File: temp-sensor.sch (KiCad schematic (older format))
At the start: 5 parts

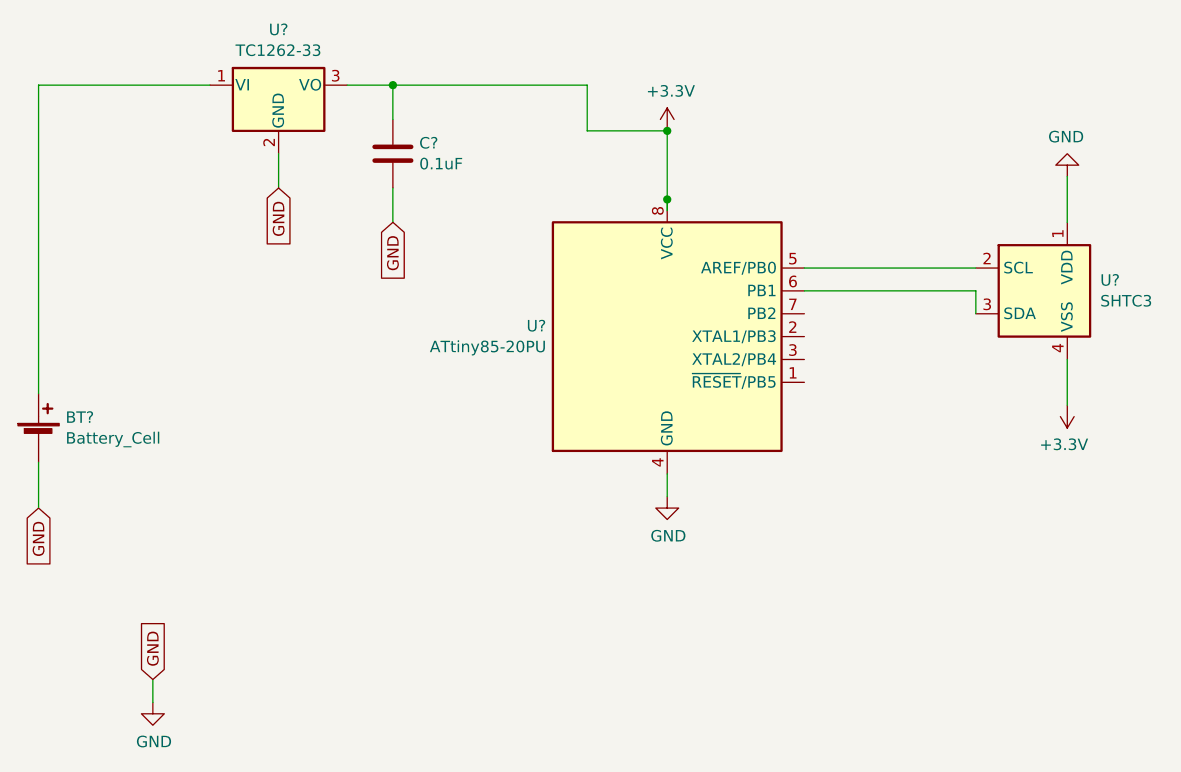
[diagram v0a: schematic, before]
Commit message: remove attiny85 (use esp01)
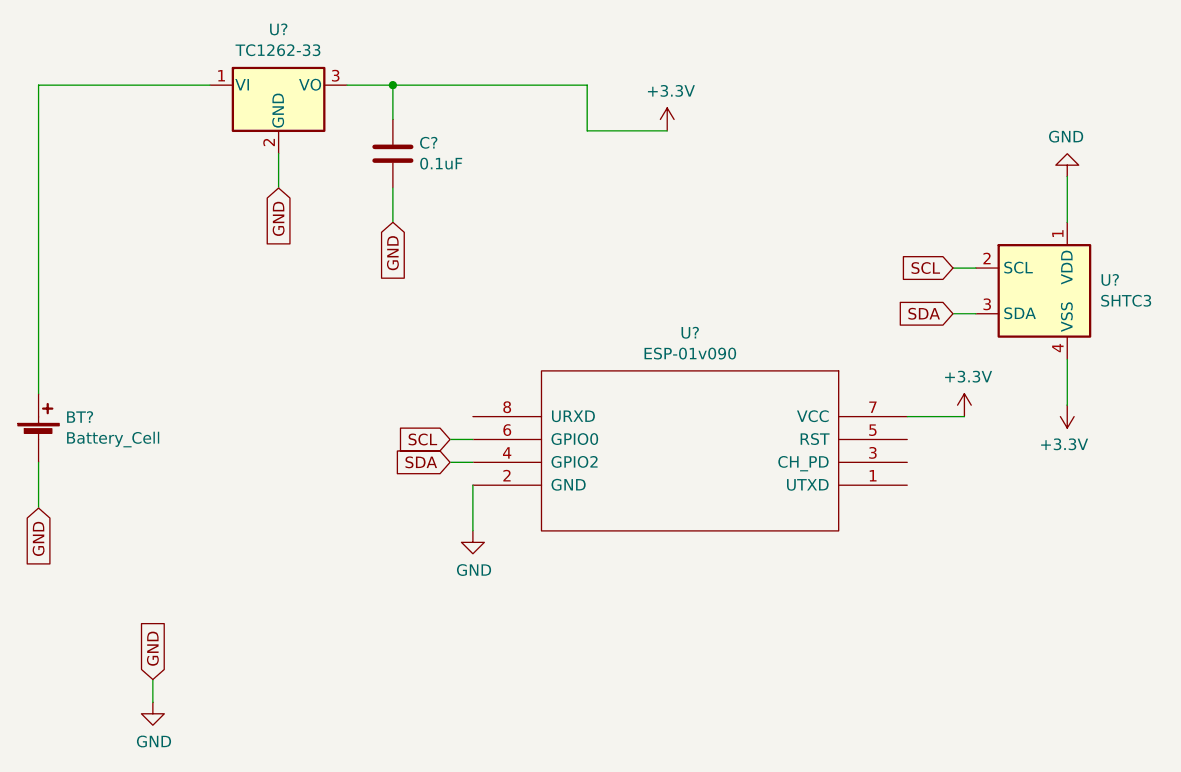
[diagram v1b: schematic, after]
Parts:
- removed U?: ATtiny85-20PU, Package_DIP:DIP-8_W7.62mm, symbol MCU_Microchip_ATtiny:ATtiny85-20PU
- added U?: ESP-01v090, symbol ESP8266:ESP-01v090
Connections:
- net labels added: SCL, SDA
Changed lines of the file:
@@
 Title "Temparature Sensor + Wifi + Attiny85"
 Date "2021-11-30"
-Rev "1"
+Rev "2"
 Comp "Kalan"
 Comment1 ""
@@
 F 3 "~" V 2000 3260 50  0001 C CNN
 	1    2000 3200
-	1    0    0    -1
-$EndComp
-$Comp
-L MCU_Microchip_ATtiny:ATtiny85-20PU U?
-U 1 1 61A69749
-P 4750 2750
-F 0 "U?" H 4221 2796 50  0000 R CNN
-F 1 "ATtiny85-20PU" H 4221 2705 50  0000 R CNN
-F 2 "Package_DIP:DIP-8_W7.62mm" H 4750 2750 50  0001 C CIN
-F 3 "http://ww1.microchip.com/downloads/en/DeviceDoc/atmel-2586-avr-8-bit-microcontroller-attiny25-attiny45-attiny85_datasheet.pdf" H 4750 2750 50  0001 C CNN
-	1    4750 2750
 	1    0    0    -1
 $EndComp
@@
 	1    0    0    -1
 $EndComp
-Wire Wire Line
-	4750 1850 4750 2150
 Text GLabel 2500 4250 1    50   Input ~ 0
 GND
@@
 Wire Wire Line
 	4400 1850 4750 1850
-Connection ~ 4750 1850
 Connection ~ 3550 1650
 Wire Wire Line
@@
 	1    0    0    -1
 $EndComp
-Connection ~ 4750 2150
-Wire Wire Line
-	4750 2150 4750 2200
-$Comp
-L power:GND #PWR?
-U 1 1 61A7129D
-P 4750 3450
-F 0 "#PWR?" H 4750 3200 50  0001 C CNN
-F 1 "GND" H 4755 3277 50  0000 C CNN
-F 2 "" H 4750 3450 50  0001 C CNN
-F 3 "" H 4750 3450 50  0001 C CNN
-	1    4750 3450
-	1    0    0    -1
-$EndComp
-Wire Wire Line
-	4750 3350 4750 3450
 $Comp
 L Sensor_Humidity:SHTC3 U?
@@
 	1    0    0    -1
 $EndComp
-Wire Wire Line
-	5350 2450 6100 2450
-Wire Wire Line
-	5350 2550 6100 2550
-Wire Wire Line
-	6100 2550 6100 2650
 $Comp
 L power:+3.3V #PWR?
@@
 Wire Wire Line
 	6500 2050 6500 2250
+$Comp
+L power:+3.3V #PWR?
+U 1 1 61A80EF4
+P 6050 3100
+F 0 "#PWR?" H 6050 2950 50  0001 C CNN
+F 1 "+3.3V" H 6065 3273 50  0000 C CNN
+F 2 "" H 6050 3100 50  0001 C CNN
+F 3 "" H 6050 3100 50  0001 C CNN
+	1    6050 3100
+	1    0    0    -1
+$EndComp
+Wire Wire Line
+	5800 3100 6050 3100
+$Comp
+L power:GND #PWR?
+U 1 1 61A81943
+P 3900 3600
+F 0 "#PWR?" H 3900 3350 50  0001 C CNN
+F 1 "GND" H 3905 3427 50  0000 C CNN
+F 2 "" H 3900 3600 50  0001 C CNN
+F 3 "" H 3900 3600 50  0001 C CNN
+	1    3900 3600
+	1    0    0    -1
+$EndComp
+Wire Wire Line
+	3900 3400 3900 3600
+$Comp
+L ESP8266:ESP-01v090 U?
+U 1 1 61A7D0E8
+P 4850 3250
+F 0 "U?" H 4850 2735 50  0000 C CNN
+F 1 "ESP-01v090" H 4850 2826 50  0000 C CNN
+F 2 "" H 4850 3250 50  0001 C CNN
+F 3 "http://l0l.org.uk/2014/12/esp8266-modules-hardware-guide-gotta-catch-em-all/" H 4850 3250 50  0001 C CNN
+	1    4850 3250
+	-1   0    0    1
+$EndComp
+Text GLabel 3800 3200 0    50   Input ~ 0
+SCL
+Text GLabel 3800 3300 0    50   Input ~ 0
+SDA
+Wire Wire Line
+	3800 3200 3900 3200
+Wire Wire Line
+	3800 3300 3900 3300
+Text GLabel 6000 2450 0    50   Input ~ 0
+SCL
+Wire Wire Line
+	6000 2450 6100 2450
+Text GLabel 6000 2650 0    50   Input ~ 0
+SDA
+Wire Wire Line
+	6000 2650 6100 2650
 $EndSCHEMATC

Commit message: update footprint
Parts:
- BT1: renamed from BT?; footprint (none) -> Battery:Battery_CR1225
- C1: renamed from C?; footprint (none) -> Capacitor_Tantalum_SMD:CP_EIA-3216-12_Kemet-S_Pad1.58x1.35mm_HandSolder
- U2: renamed from U?; footprint (none) -> ESP01
- gave numbers to parts that had none: 2
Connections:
- no-connect marks 0 -> 4
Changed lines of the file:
@@
 $EndDescr
 $Comp
-L Device:Battery_Cell BT?
+L Device:Battery_Cell BT1
 U 1 1 61A67C5E
 P 2000 3200
-F 0 "BT?" H 2118 3296 50  0000 L CNN
+F 0 "BT1" H 2118 3296 50  0000 L CNN
 F 1 "Battery_Cell" H 2118 3205 50  0000 L CNN
-F 2 "" V 2000 3260 50  0001 C CNN
+F 2 "Battery:Battery_CR1225" V 2000 3260 50  0001 C CNN
 F 3 "~" V 2000 3260 50  0001 C CNN
 	1    2000 3200
@@
 $EndComp
 $Comp
-L power:+3.3V #PWR?
+L power:+3.3V #PWR0101
 U 1 1 61A6AABD
 P 4750 1850
-F 0 "#PWR?" H 4750 1700 50  0001 C CNN
+F 0 "#PWR0101" H 4750 1700 50  0001 C CNN
 F 1 "+3.3V" H 4765 2023 50  0000 C CNN
 F 2 "" H 4750 1850 50  0001 C CNN
@@
 $EndComp
 $Comp
-L power:GND #PWR?
+L power:GND #PWR0102
 U 1 1 61A6B2A0
 P 2500 4350
-F 0 "#PWR?" H 2500 4100 50  0001 C CNN
+F 0 "#PWR0102" H 2500 4100 50  0001 C CNN
 F 1 "GND" H 2505 4177 50  0000 C CNN
 F 2 "" H 2500 4350 50  0001 C CNN
@@
 	2000 3300 2000 3500
 $Comp
-L Regulator_Linear:TC1262-33 U?
+L Regulator_Linear:TC1262-33 U1
 U 1 1 61A6D18E
 P 3050 1650
-F 0 "U?" H 3050 1892 50  0000 C CNN
+F 0 "U1" H 3050 1892 50  0000 C CNN
 F 1 "TC1262-33" H 3050 1801 50  0000 C CNN
 F 2 "" H 3050 1875 50  0001 C CIN
@@
 GND
 $Comp
-L Device:C C?
+L Device:C C1
 U 1 1 61A6F27A
 P 3550 1950
-F 0 "C?" H 3665 1996 50  0000 L CNN
+F 0 "C1" H 3665 1996 50  0000 L CNN
 F 1 "0.1uF" H 3665 1905 50  0000 L CNN
-F 2 "" H 3588 1800 50  0001 C CNN
+F 2 "Capacitor_Tantalum_SMD:CP_EIA-3216-12_Kemet-S_Pad1.58x1.35mm_HandSolder" H 3588 1800 50  0001 C CNN
 F 3 "~" H 3550 1950 50  0001 C CNN
 	1    3550 1950
@@
 $EndComp
 $Comp
-L Sensor_Humidity:SHTC3 U?
+L Sensor_Humidity:SHTC3 U3
 U 1 1 61A76649
 P 6400 2550
-F 0 "U?" H 6644 2596 50  0000 L CNN
+F 0 "U3" H 6644 2596 50  0000 L CNN
 F 1 "SHTC3" H 6644 2505 50  0000 L CNN
 F 2 "Sensor_Humidity:Sensirion_DFN-4-1EP_2x2mm_P1mm_EP0.7x1.6mm" H 6600 2200 50  0001 C CNN
@@
 $EndComp
 $Comp
-L power:+3.3V #PWR?
+L power:+3.3V #PWR0103
 U 1 1 61A799AE
 P 6500 3050
-F 0 "#PWR?" H 6500 2900 50  0001 C CNN
+F 0 "#PWR0103" H 6500 2900 50  0001 C CNN
 F 1 "+3.3V" H 6515 3223 50  0000 C CNN
 F 2 "" H 6500 3050 50  0001 C CNN
@@
 	6500 2850 6500 3050
 $Comp
-L power:GND #PWR?
+L power:GND #PWR0104
 U 1 1 61A7A14B
 P 6500 2050
-F 0 "#PWR?" H 6500 1800 50  0001 C CNN
+F 0 "#PWR0104" H 6500 1800 50  0001 C CNN
 F 1 "GND" H 6505 1877 50  0000 C CNN
 F 2 "" H 6500 2050 50  0001 C CNN
@@
 	6500 2050 6500 2250
 $Comp
-L power:+3.3V #PWR?
+L power:+3.3V #PWR0105
 U 1 1 61A80EF4
 P 6050 3100
-F 0 "#PWR?" H 6050 2950 50  0001 C CNN
+F 0 "#PWR0105" H 6050 2950 50  0001 C CNN
 F 1 "+3.3V" H 6065 3273 50  0000 C CNN
 F 2 "" H 6050 3100 50  0001 C CNN
@@
 	5800 3100 6050 3100
 $Comp
-L power:GND #PWR?
+L power:GND #PWR0106
 U 1 1 61A81943
 P 3900 3600
-F 0 "#PWR?" H 3900 3350 50  0001 C CNN
+F 0 "#PWR0106" H 3900 3350 50  0001 C CNN
 F 1 "GND" H 3905 3427 50  0000 C CNN
 F 2 "" H 3900 3600 50  0001 C CNN
@@
 	3900 3400 3900 3600
 $Comp
-L ESP8266:ESP-01v090 U?
+L ESP8266:ESP-01v090 U2
 U 1 1 61A7D0E8
 P 4850 3250
-F 0 "U?" H 4850 2735 50  0000 C CNN
+F 0 "U2" H 4850 2735 50  0000 C CNN
 F 1 "ESP-01v090" H 4850 2826 50  0000 C CNN
-F 2 "" H 4850 3250 50  0001 C CNN
+F 2 "ESP01" H 4850 3250 50  0001 C CNN
 F 3 "http://l0l.org.uk/2014/12/esp8266-modules-hardware-guide-gotta-catch-em-all/" H 4850 3250 50  0001 C CNN
 	1    4850 3250
@@
 Wire Wire Line
 	6000 2650 6100 2650
+NoConn ~ 5800 3200
+NoConn ~ 5800 3300
+NoConn ~ 5800 3400
+NoConn ~ 3900 3100
 $EndSCHEMATC

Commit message: add missing footprint
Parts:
- U2: footprint ESP01 -> ESP8266:ESP01
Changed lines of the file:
@@
 F 0 "U2" H 4850 2735 50  0000 C CNN
 F 1 "ESP-01v090" H 4850 2826 50  0000 C CNN
-F 2 "ESP01" H 4850 3250 50  0001 C CNN
+F 2 "ESP8266:ESP01" H 4850 3250 50  0001 C CNN
 F 3 "http://l0l.org.uk/2014/12/esp8266-modules-hardware-guide-gotta-catch-em-all/" H 4850 3250 50  0001 C CNN
 	1    4850 3250

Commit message: update
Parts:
- C1: footprint Capacitor_Tantalum_SMD:CP_EIA-3216-12_Kemet-S_Pad1.58x1.35mm_HandSolder -> TPCL105M010R5000:CAPC1608X90
- U1: footprint (none) -> TC1262-3:SOT-223-3
- U2: footprint ESP8266:ESP01 -> ESP8266:ESP-01; symbol ESP8266:ESP-01v090 -> temp-sensor-rescue:ESP-01v090-ESP8266
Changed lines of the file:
@@
 F 0 "U1" H 3050 1892 50  0000 C CNN
 F 1 "TC1262-33" H 3050 1801 50  0000 C CNN
-F 2 "" H 3050 1875 50  0001 C CIN
+F 2 "TC1262-3:SOT-223-3" H 3050 1875 50  0001 C CIN
 F 3 "http://ww1.microchip.com/downloads/en/DeviceDoc/21373C.pdf" H 3050 1350 50  0001 C CNN
 	1    3050 1650
@@
 F 0 "C1" H 3665 1996 50  0000 L CNN
 F 1 "0.1uF" H 3665 1905 50  0000 L CNN
-F 2 "Capacitor_Tantalum_SMD:CP_EIA-3216-12_Kemet-S_Pad1.58x1.35mm_HandSolder" H 3588 1800 50  0001 C CNN
+F 2 "TPCL105M010R5000:CAPC1608X90" H 3588 1800 50  0001 C CNN
 F 3 "~" H 3550 1950 50  0001 C CNN
 	1    3550 1950
@@
 	3900 3400 3900 3600
 $Comp
-L ESP8266:ESP-01v090 U2
+L temp-sensor-rescue:ESP-01v090-ESP8266 U2
 U 1 1 61A7D0E8
 P 4850 3250
 F 0 "U2" H 4850 2735 50  0000 C CNN
 F 1 "ESP-01v090" H 4850 2826 50  0000 C CNN
-F 2 "ESP8266:ESP01" H 4850 3250 50  0001 C CNN
+F 2 "ESP8266:ESP-01" H 4850 3250 50  0001 C CNN
 F 3 "http://l0l.org.uk/2014/12/esp8266-modules-hardware-guide-gotta-catch-em-all/" H 4850 3250 50  0001 C CNN
 	1    4850 3250
